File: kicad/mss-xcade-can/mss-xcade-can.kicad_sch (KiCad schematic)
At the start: 12 parts, among them J1 Conn_02x03_Odd_Even, J2 8P8C, J3 8P8C, U1 TCAN1042

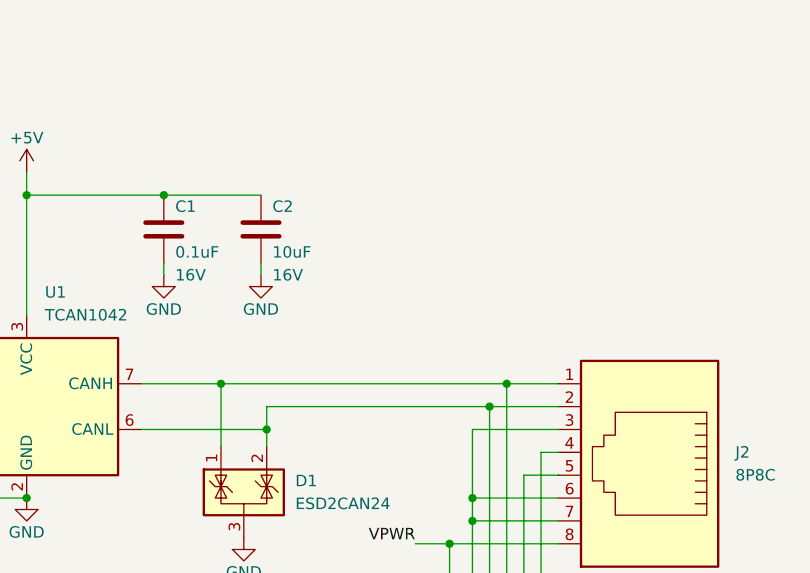
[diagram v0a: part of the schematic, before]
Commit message: Add optional termination resistor
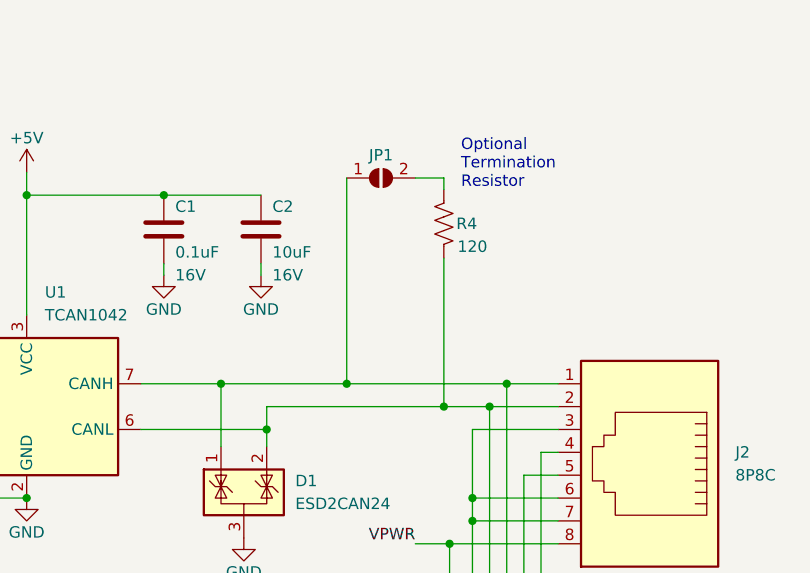
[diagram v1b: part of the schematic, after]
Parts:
- added JP1: SolderJumper_2_Open, Jumper:SolderJumper-2_P1.3mm_Open_RoundedPad1.0x1.5mm, symbol Jumper:SolderJumper_2_Open
- added R4: 120, Resistor_SMD:R_0805_2012Metric, symbol Device:R_US
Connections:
- net at D1.1 (K), J2.1, J3.1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: now also JP1.1 (A)
- net at D1.2 (K), J2.2, J3.2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: now also R4.1
- new net: JP1.2 (B), R4.2
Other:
- note added: "Optional Termination Resistor"
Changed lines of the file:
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@@
     (company "Iowa Scaled Engineering")
   )
+  (junction (at 168.275 77.47) (diameter 0) (color 0 0 0 0)
+  )
   (junction (at 159.385 82.55) (diameter 0) (color 0 0 0 0)
   )
@@
   (junction (at 154.305 77.47) (diameter 0) (color 0 0 0 0)
   )
+  (junction (at 179.07 80.01) (diameter 0) (color 0 0 0 0)
+  )
   (junction (at 182.245 119.38) (diameter 0) (color 0 0 0 0)
   )
@@
     (stroke (width 0) (type default) (color 0 0 0 0))
   )
+  (wire (pts (xy 168.275 54.61) (xy 168.275 77.47))
+    (stroke (width 0) (type default) (color 0 0 0 0))
+  )
   (wire (pts (xy 132.715 56.515) (xy 147.955 56.515))
     (stroke (width 0) (type default) (color 0 0 0 0))
@@
     (stroke (width 0) (type default) (color 0 0 0 0))
   )
-  (wire (pts (xy 154.305 77.47) (xy 186.055 77.47))
+  (wire (pts (xy 154.305 77.47) (xy 168.275 77.47))
     (stroke (width 0) (type default) (color 0 0 0 0))
   )
@@
     (stroke (width 0) (type default) (color 0 0 0 0))
   )
+  (wire (pts (xy 179.07 63.5) (xy 179.07 80.01))
+    (stroke (width 0) (type default) (color 0 0 0 0))
+  )
   (wire (pts (xy 182.245 111.76) (xy 191.77 111.76))
     (stroke (width 0) (type default) (color 0 0 0 0))
@@
     (stroke (width 0) (type default) (color 0 0 0 0))
   )
+  (wire (pts (xy 179.07 54.61) (xy 179.07 55.88))
+    (stroke (width 0) (type default) (color 0 0 0 0))
+  )
   (wire (pts (xy 182.245 111.76) (xy 182.245 119.38))
     (stroke (width 0) (type default) (color 0 0 0 0))
@@
     (stroke (width 0) (type default) (color 0 0 0 0))
   )
+  (wire (pts (xy 168.275 77.47) (xy 186.055 77.47))
+    (stroke (width 0) (type default) (color 0 0 0 0))
+  )
   (wire (pts (xy 50.165 59.055) (xy 50.165 57.15))
     (stroke (width 0) (type default) (color 0 0 0 0))
@@
     (stroke (width 0) (type default) (color 0 0 0 0))
   )
+  (wire (pts (xy 175.895 54.61) (xy 179.07 54.61))
+    (stroke (width 0) (type default) (color 0 0 0 0))
+  )
+  (wire (pts (xy 179.07 80.01) (xy 184.15 80.01))
+    (stroke (width 0) (type default) (color 0 0 0 0))
+  )
   (wire (pts (xy 182.245 121.92) (xy 182.245 128.905))
     (stroke (width 0) (type default) (color 0 0 0 0))
@@
     (stroke (width 0) (type default) (color 0 0 0 0))
   )
-  (wire (pts (xy 159.385 80.01) (xy 184.15 80.01))
+  (wire (pts (xy 159.385 80.01) (xy 179.07 80.01))
     (stroke (width 0) (type default) (color 0 0 0 0))
   )
@@
   (text "LCC/CMRI Expansion\nConnector" (at 59.69 43.18 180)
     (effects (font (size 1.27 1.27)) (justify right bottom))
+  )
+  (text "Optional\nTermination\nResistor" (at 180.975 55.88 0)
+    (effects (font (size 1.27 1.27)) (justify left bottom))
   )
   (text "LCC Pinout\n-------------\n1 - CAN_H\n2 - CAN_L\n3 - CAN_GND\n4 - ALT_L\n5 - ALT_H\n6 - CAN_SHIELD\n7 - PWR_NEG\n8 - PWR_POS\n"
@@
     (pin "1")
   )
+  (symbol (lib_id "Device:R_US") (at 179.07 59.69 0) (mirror x) (unit 1)
+    (in_bom yes) (on_board yes)
+    (property "Reference" "R4" (id 0) (at 181.61 59.69 0))
+    (property "Value" "120" (id 1) (at 182.245 62.23 0))
+    (property "Footprint" "Resistor_SMD:R_0805_2012Metric" (id 2) (at 180.086 59.436 90)
+      (effects (font (size 1.27 1.27)) hide)
+    )
+    (property "Datasheet" "~" (id 3) (at 179.07 59.69 0)
+      (effects (font (size 1.27 1.27)) hide)
+    )
+    (pin "1")
+    (pin "2")
+  )
   (symbol (lib_id "power:+5V") (at 48.895 50.165 0) (unit 1)
     (in_bom yes) (on_board yes)
@@
     (pin "1")
   )
+  (symbol (lib_id "Jumper:SolderJumper_2_Open") (at 172.085 54.61 0) (unit 1)
+    (in_bom yes) (on_board yes)
+    (property "Reference" "JP1" (id 0) (at 172.085 52.07 0))
+    (property "Value" "SolderJumper_2_Open" (id 1) (at 172.085 52.07 0)
+      (effects (font (size 1.27 1.27)) hide)
+    )
+    (property "Footprint" "Jumper:SolderJumper-2_P1.3mm_Open_RoundedPad1.0x1.5mm" (id 2) (at 172.085 54.61 0)
+      (effects (font (size 1.27 1.27)) hide)
+    )
+    (property "Datasheet" "~" (id 3) (at 172.085 54.61 0)
+      (effects (font (size 1.27 1.27)) hide)
+    )
+    (pin "1")
+    (pin "2")
+  )
   (symbol (lib_id "ISE_Generic:TCAN1042") (at 132.715 80.01 0) (unit 1)
     (in_bom yes) (on_board yes) (fields_autoplaced)
@@
       (reference "J3") (unit 1) (value "8P8C") (footprint "RJ45_Amphenol_54602-x08_Horizontal")
     )
+    (path "/f2b71306-58a2-4798-ba5a-d80b9bb63591"
+      (reference "JP1") (unit 1) (value "SolderJumper_2_Open") (footprint "Jumper:SolderJumper-2_P1.3mm_Open_RoundedPad1.0x1.5mm")
+    )
     (path "/80fd322c-fee8-4bb3-a4dc-ff19a2c95993"
       (reference "R1") (unit 1) (value "1k") (footprint "Resistor_SMD:R_0805_2012Metric")
@@
       (reference "R3") (unit 1) (value "1k") (footprint "Resistor_SMD:R_0805_2012Metric")
     )
+    (path "/92c4c457-bc78-48a5-bd50-4bd24ca88129"
+      (reference "R4") (unit 1) (value "120") (footprint "Resistor_SMD:R_0805_2012Metric")
+    )
     (path "/f749106f-e6f3-48cf-abab-6fb4435b481c"
